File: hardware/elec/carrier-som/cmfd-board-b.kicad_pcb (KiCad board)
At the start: 2 copper layers, 120 x 90 mm, 22 parts, among them J10 SoM_A, J11 SoM_B, J2 B2B_A, J3 USB-C_PD, J4 USB-C_AUX, J5 Ethernet, J6 CAN_UART, J7 AUDIO, J8 BAT, U11 REG_3V3, U12 REG_5V, U6 ISO1042

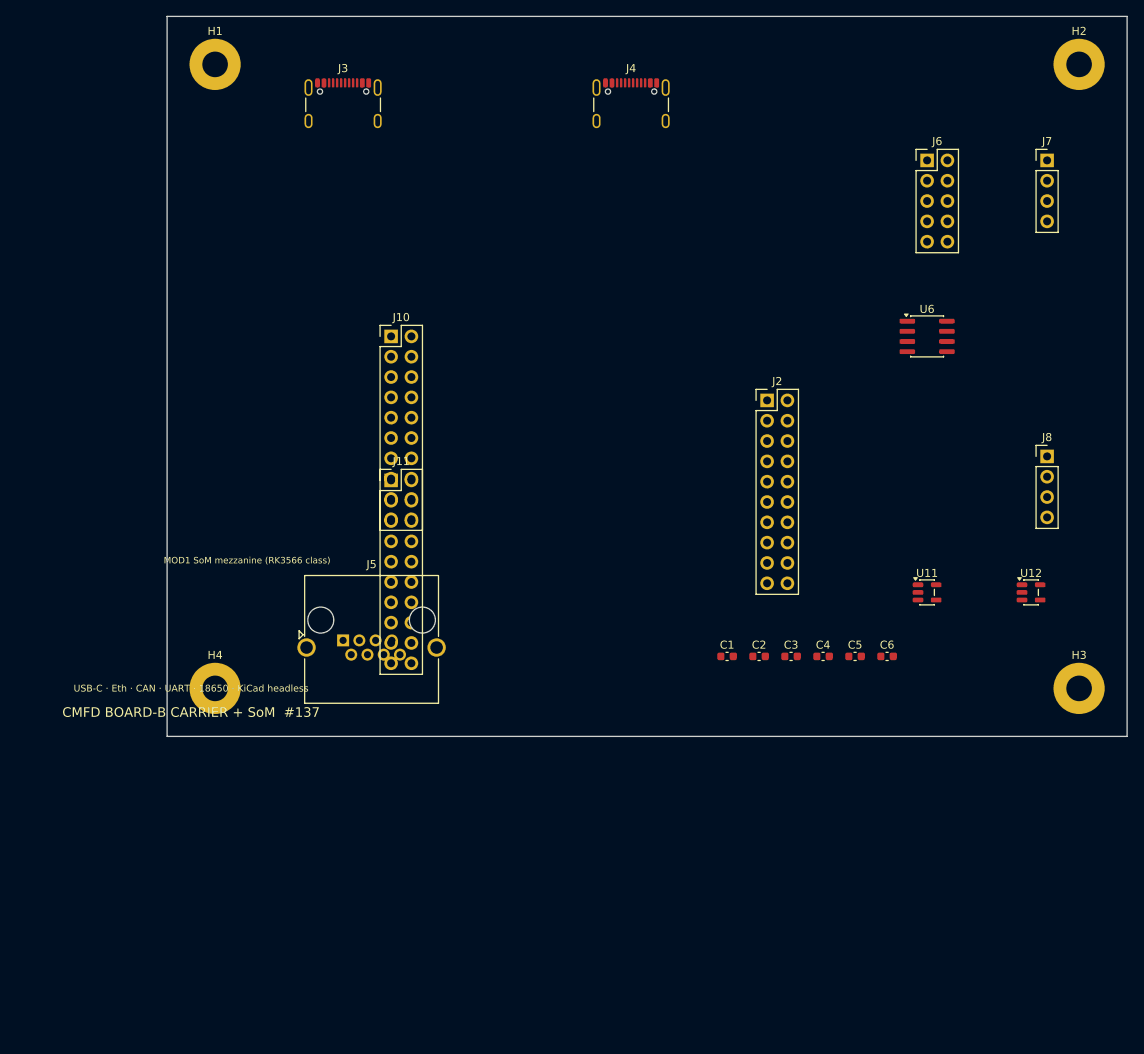
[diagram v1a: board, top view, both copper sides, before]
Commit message: feat(hardware): fab-ready passive bezel PCB + plain-language order guide
Board A is a switch-only panel: one pin per button, short tracks, zero
copper shorts on DRC. ORDER-THIS.md explains what to upload to JLCPCB and
the print shop with no KiCad steps.

Refs: #137
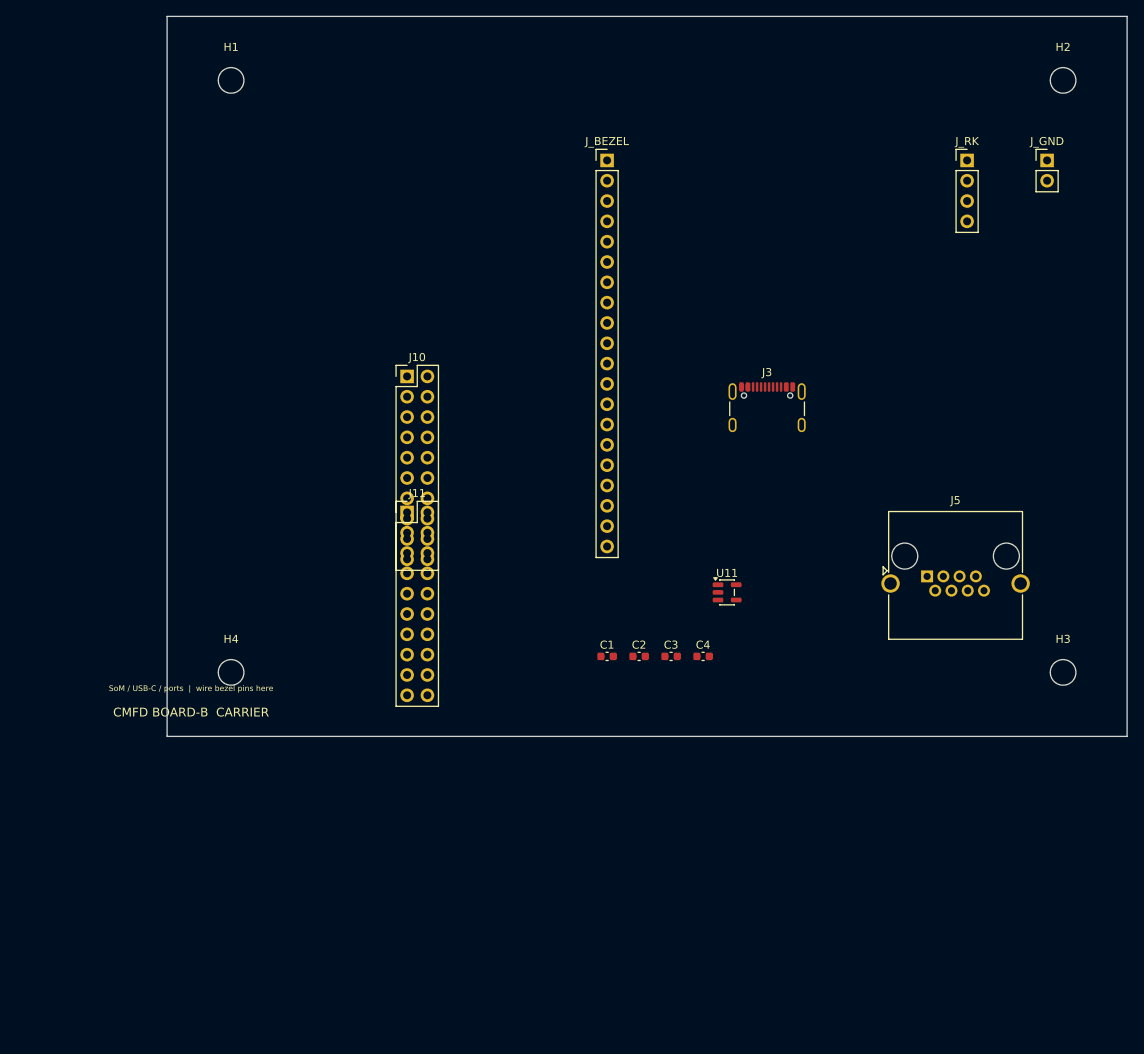
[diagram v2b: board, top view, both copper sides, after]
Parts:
- removed C5, C6: 100nF, C_0603_1608Metric
- removed J2: B2B_A, PinHeader_2x10_P2.54mm_Vertical
- removed J4: USB-C_AUX, USB_C_Receptacle_GCT_USB4105-xx-A_16P_TopMnt_Horizontal
- removed J6: CAN_UART, PinHeader_2x05_P2.54mm_Vertical
- removed J7: AUDIO, PinHeader_1x04_P2.54mm_Vertical
- removed J8: BAT, PinHeader_1x04_P2.54mm_Vertical
- removed U12: REG_5V, SOT-23-5
- removed U6: ISO1042, SOIC-8_3.9x4.9mm_P1.27mm
- added J_BEZEL: OSB1-20, PinHeader_1x20_P2.54mm_Vertical, F.Cu at (55.0, 18.0)
- added J_GND: GND, PinHeader_1x02_P2.54mm_Vertical, F.Cu at (110.0, 18.0)
- added J_RK: rockers, PinHeader_1x04_P2.54mm_Vertical, F.Cu at (100.0, 18.0)
- H1, H2, H3, H4: footprint MountingHole_3.2mm_M3_Pad -> MountingHole_3.2mm_M3
- J3: value USB-C_PD -> USB-C
- J5: value Ethernet -> Eth
- U11: value REG_3V3 -> 3V3
- moved J5 73.4 mm to (95.0, 70.0)
- moved J3 65.2 mm to (75.0, 50.0)
- moved U11 25.0 mm to (70.0, 72.0)
- moved C1 15.0 mm to (55.0, 80.0)
- moved C2 15.0 mm to (59.0, 80.0)
- moved C3 15.0 mm to (63.0, 80.0)
- moved C4 15.0 mm to (67.0, 80.0)
- moved J10 5.39 mm to (30.0, 45.0)
- moved J11 4.47 mm to (30.0, 62.0)
- moved H1 2.83 mm to (8.00, 8.00)
- moved H2 2.83 mm to (112.0, 8.00)
- moved H3 2.83 mm to (112.0, 82.0)
- moved H4 2.83 mm to (8.00, 82.0)
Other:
- board text added: "CMFD BOARD-B CARRIER"
- board text added: "SoM / USB-C / ports | wire bezel pins here"
- board text removed: "CMFD BOARD-B CARRIER + SoM #137"
- board text removed: "MOD1 SoM mezzanine (RK3566 class)"
- board text removed: "USB-C · Eth · CAN · UART · 18650 · KiCad headless"

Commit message: fix(hardware): rockers clear glass, edge ports, M12, RA headers
- Rockers moved to pure corners (16 mm inset, 12×9 cap) so caps never
  enter the 102 mm glass aperture; OpenSCAD + KiCad + viewer aligned
- Board B USB-C / RJ45 / harness moved to front edge (not board center)
- Three M12 panel bulkheads on case left wall; J_M12 edge harness on B
- Board A uses right-angle 1-pin headers (outward); pins no longer
  taller than the 4.3 mm tact switches
- Rebuilt STLs, Gerbers, KiCad raytraces, Blender studio shots

Refs: #137
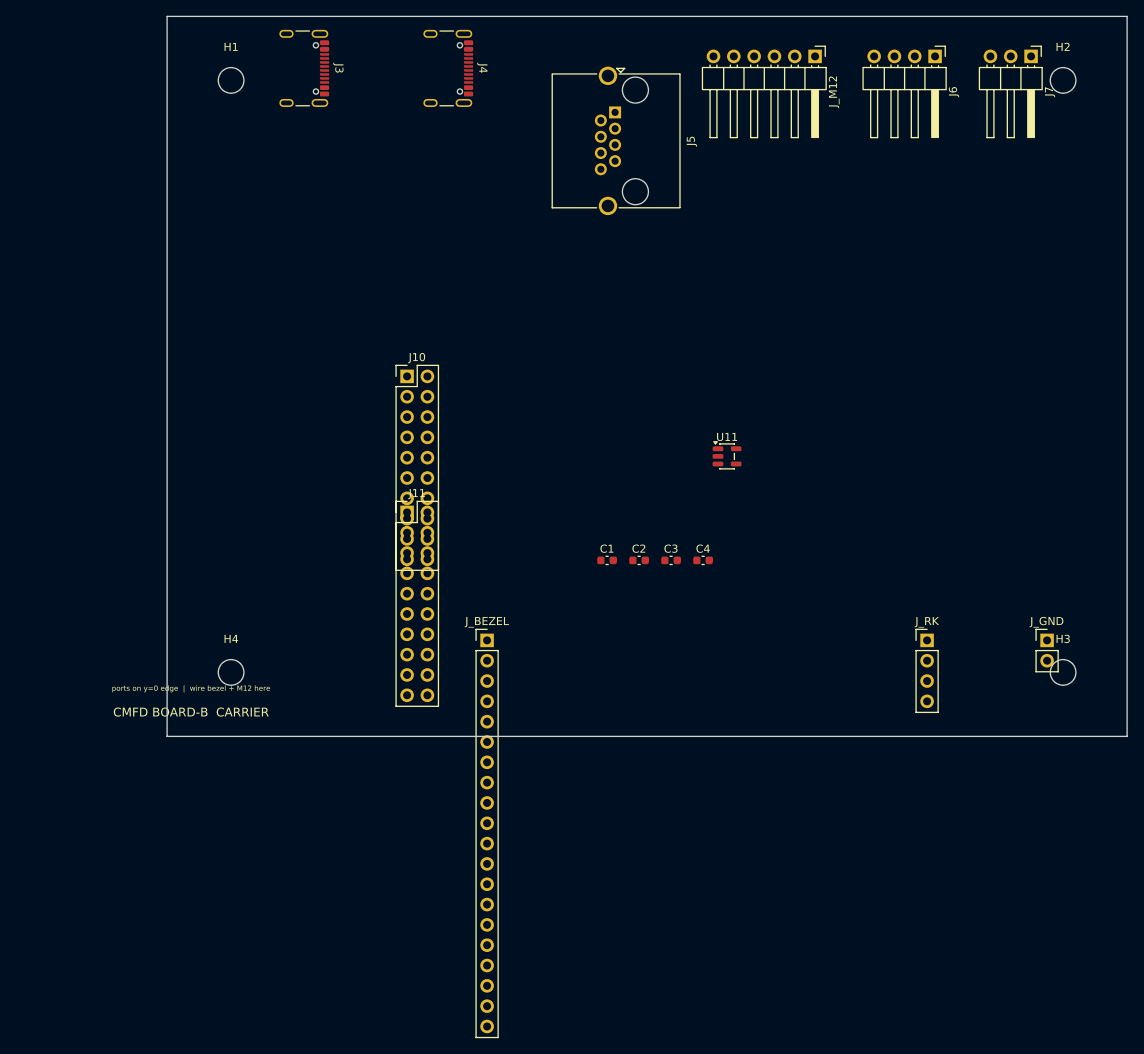
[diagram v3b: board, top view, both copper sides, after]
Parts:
- added J4: USB-C data, USB_C_Receptacle_GCT_USB4105-xx-A_16P_TopMnt_Horizontal, F.Cu at (34.0, 6.50)
- added J6: CAN/UART, PinHeader_1x04_P2.54mm_Horizontal, F.Cu at (96.0, 5.00)
- added J7: Audio, PinHeader_1x03_P2.54mm_Horizontal, F.Cu at (108.0, 5.00)
- added J_M12: M12 harness, PinHeader_1x06_P2.54mm_Horizontal, F.Cu at (81.0, 5.00)
- J3: value USB-C -> USB-C charge
- moved J3 73.3 mm to (16.0, 6.50), turned to -90 degrees
- moved J5 69.9 mm to (56.0, 12.0), turned to -90 degrees
- moved J_BEZEL 61.8 mm to (40.0, 78.0)
- moved J_RK 60.2 mm to (95.0, 78.0)
- moved J_GND 60.0 mm to (110.0, 78.0)
- moved U11 17.0 mm to (70.0, 55.0)
- moved C1 12.0 mm to (55.0, 68.0)
- moved C2 12.0 mm to (59.0, 68.0)
- moved C3 12.0 mm to (63.0, 68.0)
- moved C4 12.0 mm to (67.0, 68.0)
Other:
- board text added: "ports on y=0 edge | wire bezel + M12 here"
- board text removed: "SoM / USB-C / ports | wire bezel pins here"
